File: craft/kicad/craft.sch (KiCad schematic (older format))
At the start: 33 parts, among them U1 LM2596T-5

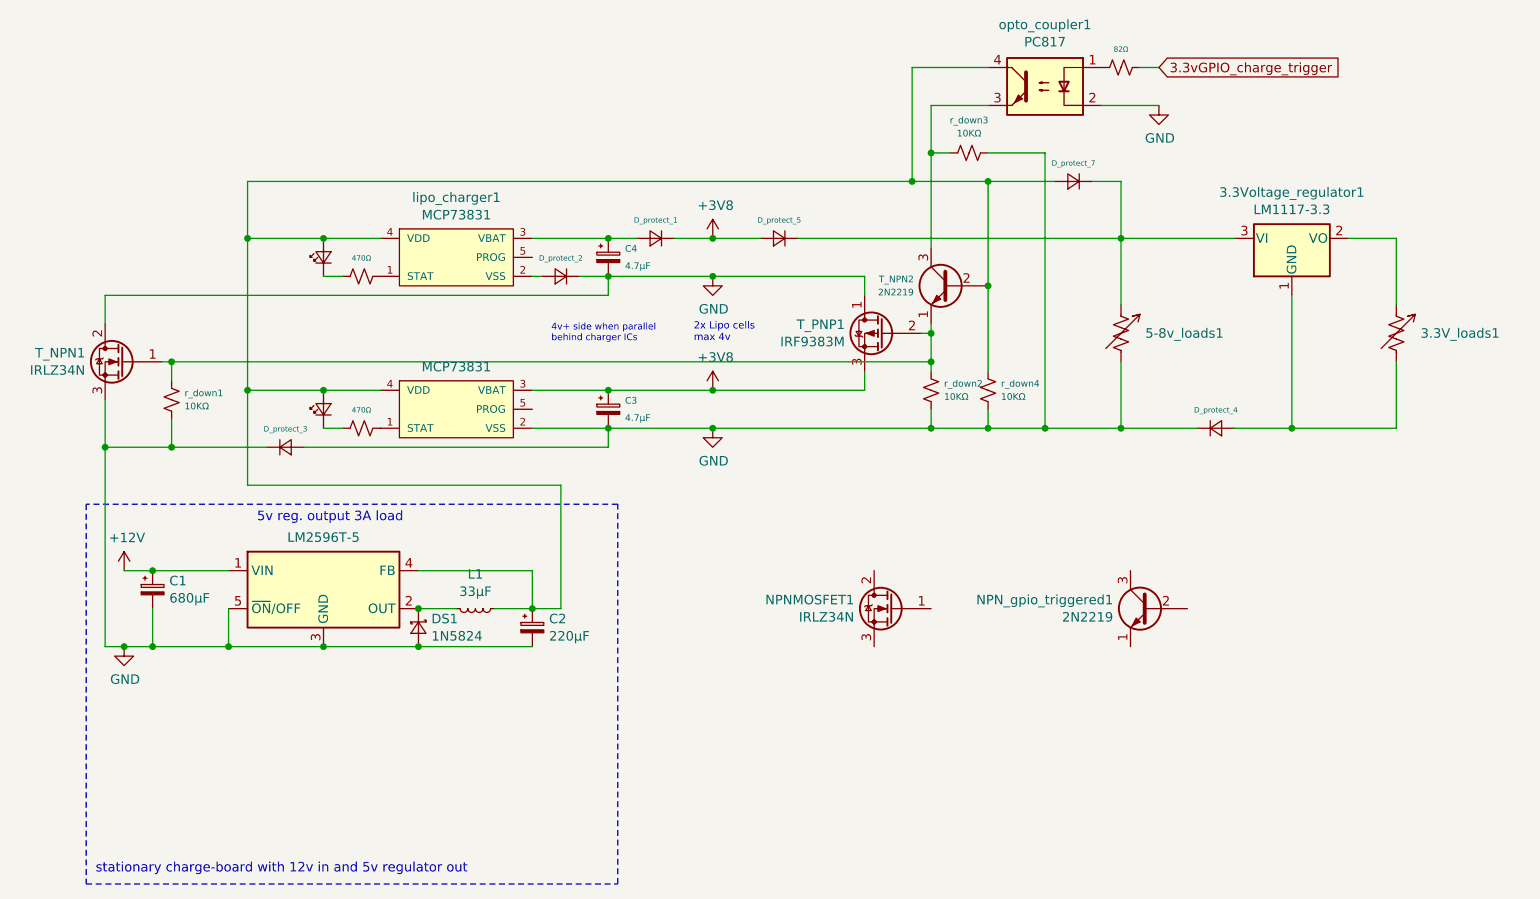
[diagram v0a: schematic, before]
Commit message: Reduces complexity of the charge circuit
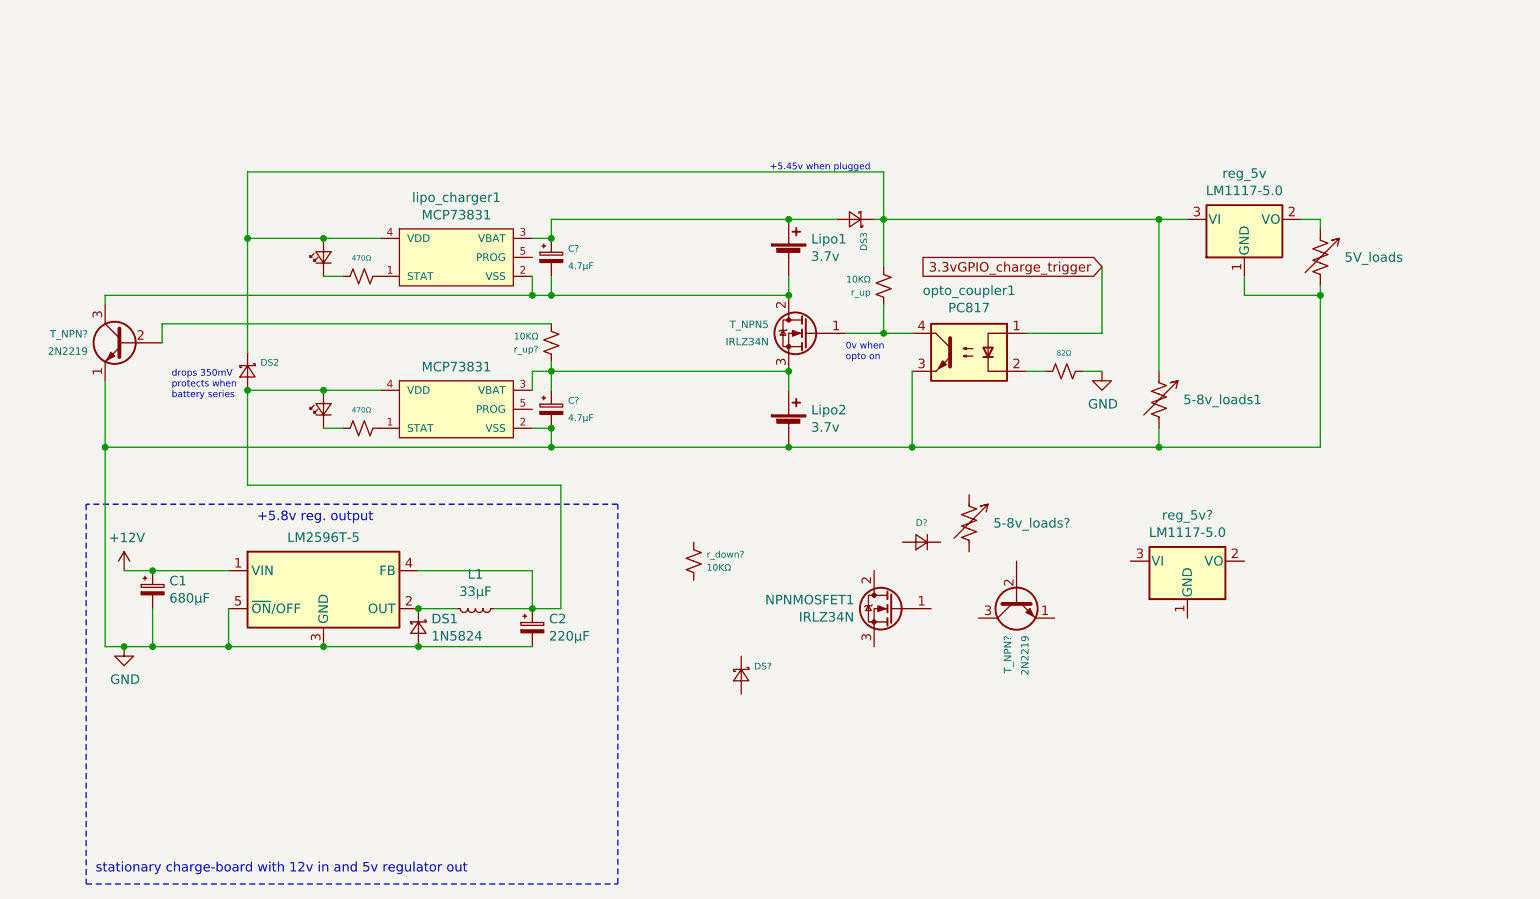
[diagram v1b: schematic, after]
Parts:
- removed 3.3Voltage_regulator1: LM1117-3.3, symbol Regulator_Linear:LM1117-3.3
- removed C3, C4: 4.7μF, symbol Device:CP_Small
- removed D_protect_1, D_protect_2, D_protect_3, D_protect_4, D_protect_5, D_protect_7: D_Small, symbol Device:D_Small
- removed NPN_gpio_triggered1, T_NPN2: 2N2219, Package_TO_SOT_THT:TO-39-3, symbol Transistor_BJT:2N2219
- removed T_NPN1: IRLZ34N, Package_TO_SOT_THT:TO-220-3_Vertical, symbol Transistor_FET:IRLZ34N
- removed T_PNP1: IRF9383M, Package_DirectFET:DirectFET_MX, symbol Transistor_FET:IRF9383M
- removed r_diode1: 82Ω, symbol Device:R_Small_US
- removed r_down1, r_down2, r_down3, r_down4: 10KΩ, symbol Device:R_Small_US
- added 5-8v_loads?: R_Variable_US, symbol Device:R_Variable_US
- added C? (x2): 4.7μF, symbol Device:CP_Small
- added D?: D_Small, symbol Device:D_Small
- added DS2, DS3, DS?: 1N5824, symbol Device:D_Schottky_Small
- added Lipo1, Lipo2: 3.7v, symbol Device:Battery_Cell
- added T_NPN5: IRLZ34N, Package_TO_SOT_THT:TO-220-3_Vertical, symbol Transistor_FET:IRLZ34N
- added T_NPN? (x2): 2N2219, Package_TO_SOT_THT:TO-39-3, symbol Transistor_BJT:2N2219
- added r_diode?: 82Ω, symbol Device:R_Small_US
- added r_down?, r_up, r_up?: 10KΩ, symbol Device:R_Small_US
- added reg_5v, reg_5v?: LM1117-5.0, symbol Regulator_Linear:LM1117-5.0
- renumbered 3.3V_loads1 to 5V_loads
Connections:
- net 3.3vGPIO_charge_trigger: now also opto_coupler1.1
- net GND: now also 5V_loads.2, opto_coupler1.3, C?.2, Lipo2.2 (-), T_NPN?.1 (E), r_diode?.2, reg_5v.1 (GND); no longer opto_coupler1.2
- net at lipo_charger1.2 (VSS): now also C?.2, Lipo1.2 (-), T_NPN5.2 (D), T_NPN?.3 (C)
- net at lipo_charger1.3 (VBAT): now also C?.1, DS3.2 (A), Lipo1.1 (+)
- net at C2.1, D_charge_stat_2.2 (A), L1.1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: now also DS2.2 (A); no longer D_charge_stat_1.2 (A), lipo_charger1.4 (VDD), opto_coupler1.4
- net at 5-8v_loads1.1: now also D_charge_stat_1.2 (A), lipo_charger1.4 (VDD), DS2.1 (K), DS3.1 (K), r_up.1, reg_5v.3 (VI)
- net at 5V_loads.1: now also reg_5v.2 (VO)
- net +3V8: no longer names the net of lipo_charger2.3 (VBAT)
- net +3V8: now also C?.1, Lipo2.1 (+), T_NPN5.3 (S), r_up?.2
- new net: opto_coupler1.2, r_diode?.1
- new net: T_NPN5.1 (G), opto_coupler1.4, r_up.2
- new net: T_NPN?.2 (B), r_up?.1
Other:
- note added: "+5.45v when plugged"
- note added: "+5.8v reg. output"
- note added: "0v when\nopto on"
- note added: "drops 350mV\nprotects when\nbattery series"
- note removed: "2x Lipo cells\nmax 4v"
- note removed: "4v+ side when parallel\nbehind charger ICs"
- note removed: "5v reg. output 3A load"
- moved on the sheet: 5-8v_loads1, 5V_loads, opto_coupler1
